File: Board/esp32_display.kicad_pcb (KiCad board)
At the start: 2 copper layers, 90.5 x 69 mm, 57 parts, among them J1 Conn_01x06_Male, J2 USB_B_Micro, SW1 RST_BTN, SW2 SCREEN_OFF_BTN, U1 ESP32-WROOM-32, U2 MAX1821, U3 Display_ILI9341

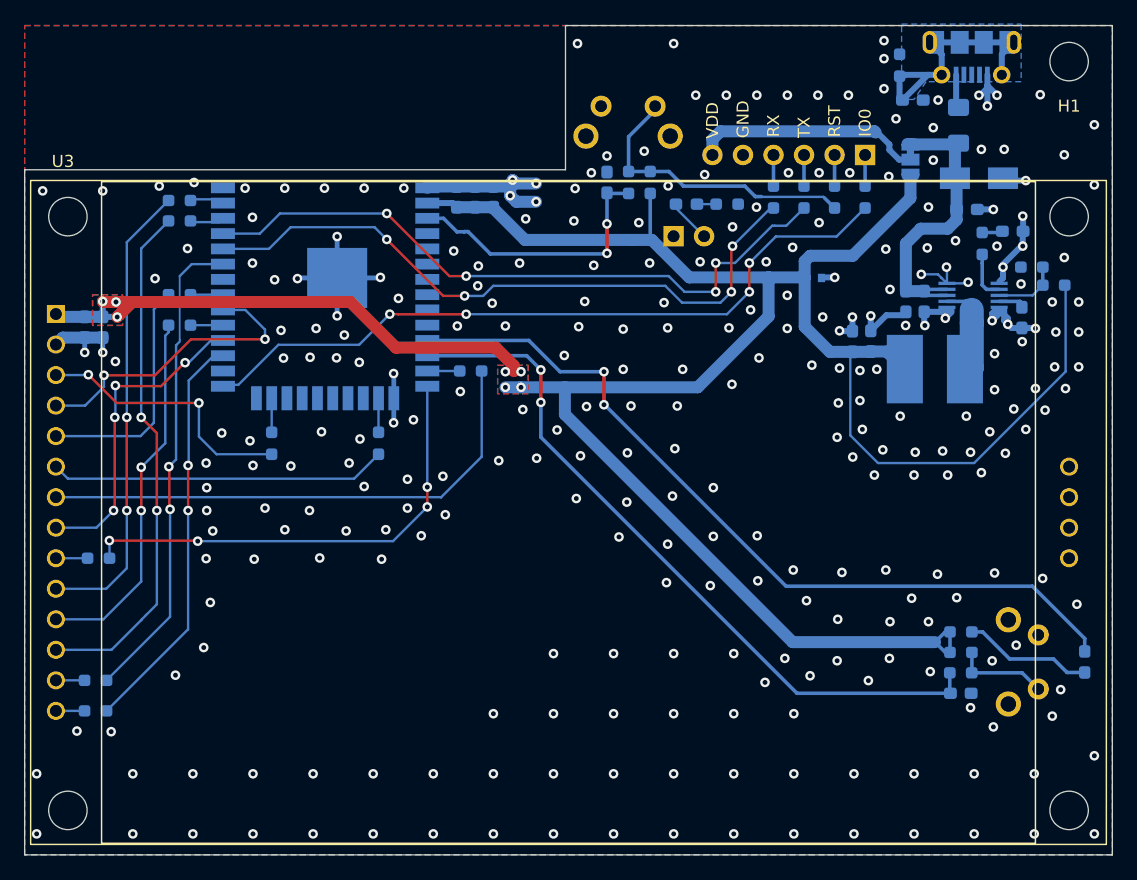
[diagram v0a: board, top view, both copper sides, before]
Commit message: Add I2C pin header
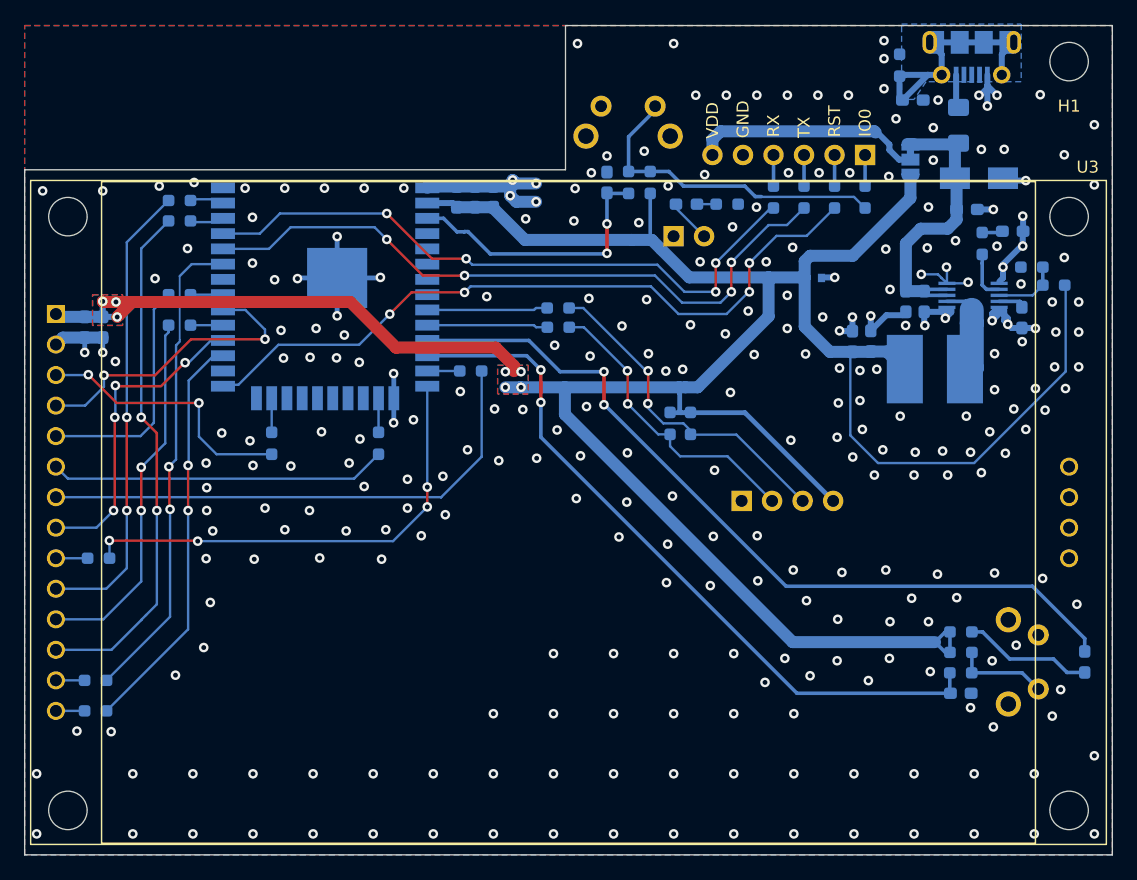
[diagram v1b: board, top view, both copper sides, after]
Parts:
- added J1: Conn_01x04_Male, Connector_PinHeader_2.54mm:PinHeader_1x04_P2.54mm_Horizontal, B.Cu at (146.7, 71.5)
- added R13: 51k, Resistor_SMD:R_0603_1608Metric_Pad0.98x0.95mm_HandSolder, B.Cu at (142.4, 65.1)
- added R14: 51k, Resistor_SMD:R_0603_1608Metric_Pad0.98x0.95mm_HandSolder, B.Cu at (140.7, 65.1)
- added R27: 220, Resistor_SMD:R_0603_1608Metric_Pad0.98x0.95mm_HandSolder, B.Cu at (131.4, 55.5)
- added R28: 220, Resistor_SMD:R_0603_1608Metric_Pad0.98x0.95mm_HandSolder, B.Cu at (131.4, 57.1)
- moved kibuzzard-61D6E91A 11.0 mm to (126.2, 81.2)
- renumbered J1 to J2, J2 to J3, R13 to R15, R14 to R16, R15 to R17, R16 to R18, R17 to R19, R18 to R20, R19 to R21, R20 to R22, R21 to R23, R22 to R24, R23 to R25, R24 to R26
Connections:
- R15 pad 1: /MCU/UART_RX -> /MCU/UART_TX
- R16 pad 1: /MCU/UART_TX -> /MCU/UART_RX
- R17 pad 1: /MCU/RST -> /MCU/IO0
- R18 pad 1: /MCU/IO0 -> /MCU/RST
- U1 pad 10: unconnected-(U1-Pad10) -> /MCU/I2C_SDA
- U1 pad 9: unconnected-(U1-Pad9) -> /MCU/I2C_SCL
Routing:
- net Net-(J1-Pad3): track 0.00 -> 27.9 mm, vias 0 -> 2
- net Net-(J1-Pad2): track 0.00 -> 25.0 mm, vias 0 -> 2
- net +3V3: track 222.6 -> 240.8 mm
- net /MCU/I2C_SDA: track 0.00 -> 10.1 mm
- net /MCU/I2C_SCL: track 0.00 -> 10.0 mm
- net /MCU/UART_TX: track 56.0 -> 53.5 mm
- net /MCU/RST: track 24.7 -> 27.3 mm
- net /MCU/UART_RX: track 55.3 -> 56.4 mm
- net /MCU/IO0: track 61.0 -> 60.3 mm
- net GND: vias 289 -> 280
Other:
- board text added: "CLK"
- board text added: "SDA"

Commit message: Add fiducials
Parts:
- added FID1: Fiducial, Fiducial:Fiducial_0.5mm_Mask1mm, B.Cu at (170.0, 40.0)
- added FID2: Fiducial, Fiducial:Fiducial_0.5mm_Mask1mm, B.Cu at (170.0, 97.0)
- added FID3: Fiducial, Fiducial:Fiducial_0.5mm_Mask1mm, B.Cu at (95.0, 97.0)
- renumbered J2 to J1, J1 to J2, R27 to R13, R28 to R14, R13 to R15, R14 to R16, R15 to R17, R16 to R18, R17 to R19, R18 to R20, R19 to R21, R20 to R22, R21 to R23, R22 to R24, R23 to R25, R24 to R26, R25 to R27, R26 to R28
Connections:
- net /MCU/RST renamed /MCU/nRST

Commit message: Update typo
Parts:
- L1: value 10uF -> 10uH
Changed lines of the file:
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@@
       (effects (font (size 1 1) (thickness 0.15)) (justify mirror))
     )
-    (fp_text value "10uF" (at 0 -5.08) (layer "B.Fab")
+    (fp_text value "10uH" (at 0 -5.08) (layer "B.Fab")
       (effects (font (size 1 1) (thickness 0.15)) (justify mirror))
     )
